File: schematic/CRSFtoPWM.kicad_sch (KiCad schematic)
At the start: 29 parts, among them J1 Bat+, J2 UART1/Rx, J3 ICSP, J4 TSW-104-08-G-T-RA, J5 TSW-104-08-G-T-RA, J6 TSW-104-08-G-T-RA, J7 TSW-102-08-L-T-RA, U1 AP7375-50W5-7, U2 AP2210N-3.3TRG1, U3 ATSAMD21E18A-MU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

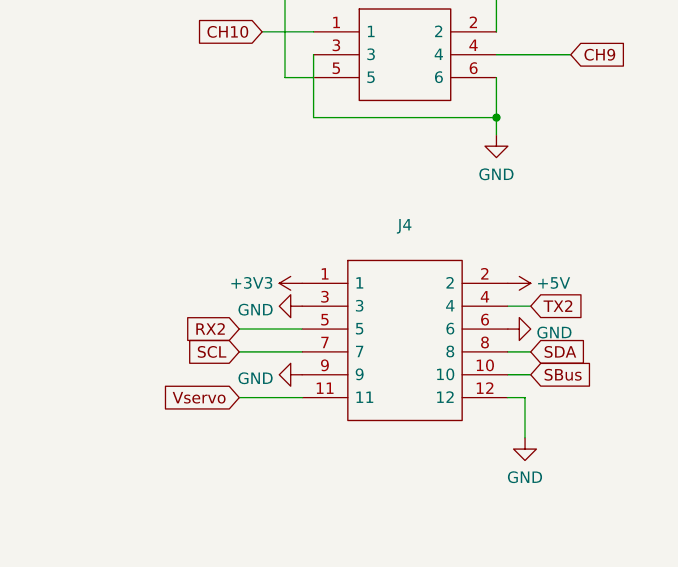
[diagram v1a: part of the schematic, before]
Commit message: Improved Vservo current capacity
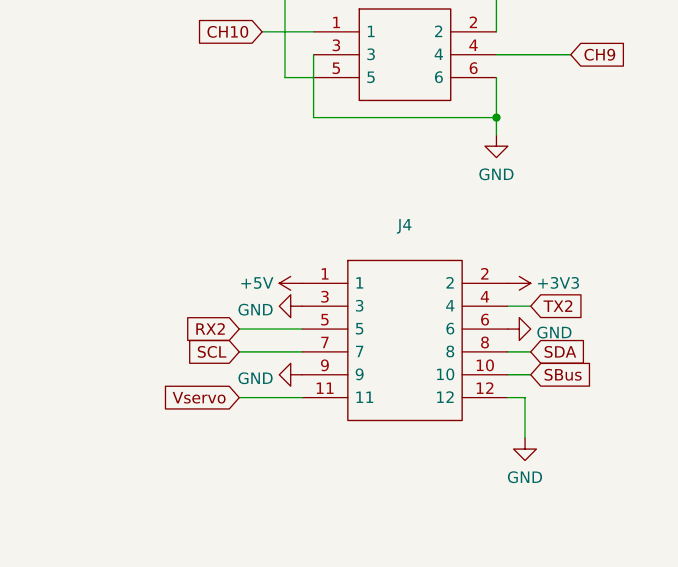
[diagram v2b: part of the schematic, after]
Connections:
- net +3V3: now also J4.2; no longer J4.1
- net +5V: now also J4.1; no longer J4.2
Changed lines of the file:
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@@
     (pin "1")
   )
-  (symbol (lib_id "power:+3V3") (at 222.885 142.875 90) (unit 1)
-    (in_bom yes) (on_board yes)
-    (property "Reference" "#PWR036" (id 0) (at 226.695 142.875 0)
-      (effects (font (size 1.27 1.27)) hide)
-    )
-    (property "Value" "+3V3" (id 1) (at 219.71 142.875 90)
-      (effects (font (size 1.27 1.27)) (justify left))
-    )
-    (property "Footprint" "" (id 2) (at 222.885 142.875 0)
-      (effects (font (size 1.27 1.27)) hide)
-    )
-    (property "Datasheet" "" (id 3) (at 222.885 142.875 0)
+  (symbol (lib_id "power:+3V3") (at 245.745 142.875 270) (unit 1)
+    (in_bom yes) (on_board yes)
+    (property "Reference" "#PWR036" (id 0) (at 241.935 142.875 0)
+      (effects (font (size 1.27 1.27)) hide)
+    )
+    (property "Value" "+3V3" (id 1) (at 248.92 142.875 90)
+      (effects (font (size 1.27 1.27)) (justify left))
+    )
+    (property "Footprint" "" (id 2) (at 245.745 142.875 0)
+      (effects (font (size 1.27 1.27)) hide)
+    )
+    (property "Datasheet" "" (id 3) (at 245.745 142.875 0)
       (effects (font (size 1.27 1.27)) hide)
     )
@@
     (pin "1")
   )
-  (symbol (lib_id "power:+5V") (at 245.745 142.875 270) (unit 1)
-    (in_bom yes) (on_board yes)
-    (property "Reference" "#PWR037" (id 0) (at 241.935 142.875 0)
-      (effects (font (size 1.27 1.27)) hide)
-    )
-    (property "Value" "+5V" (id 1) (at 248.92 142.875 90)
-      (effects (font (size 1.27 1.27)) (justify left))
-    )
-    (property "Footprint" "" (id 2) (at 245.745 142.875 0)
-      (effects (font (size 1.27 1.27)) hide)
-    )
-    (property "Datasheet" "" (id 3) (at 245.745 142.875 0)
-      (effects (font (size 1.27 1.27)) hide)
-    )
+  (symbol (lib_id "power:+5V") (at 222.885 142.875 90) (unit 1)
+    (in_bom yes) (on_board yes)
+    (property "Reference" "#PWR037" (id 0) (at 226.695 142.875 0)
+      (effects (font (size 1.27 1.27)) hide)
+    )
+    (property "Value" "+5V" (id 1) (at 219.71 142.875 90)
+      (effects (font (size 1.27 1.27)) (justify left))
+    )
+    (property "Footprint" "" (id 2) (at 222.885 142.875 0)
+      (effects (font (size 1.27 1.27)) hide)
+    )
+    (property "Datasheet" "" (id 3) (at 222.885 142.875 0)
+      (effects (font (size 1.27 1.27)) hide)
+    )

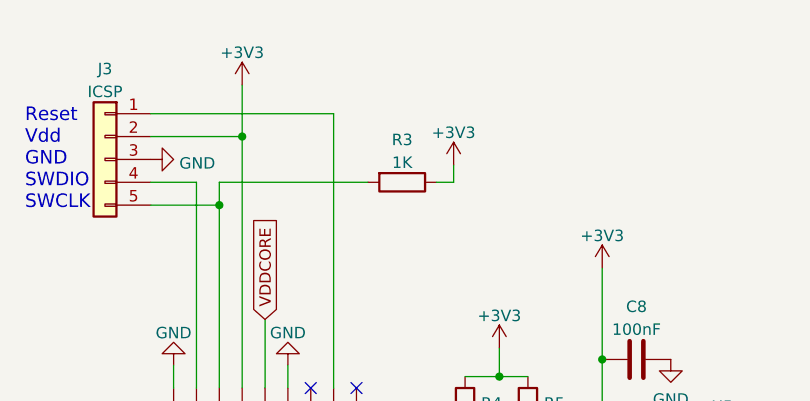
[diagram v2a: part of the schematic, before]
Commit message: Added pullup to RESET
Updated pins in Harmony
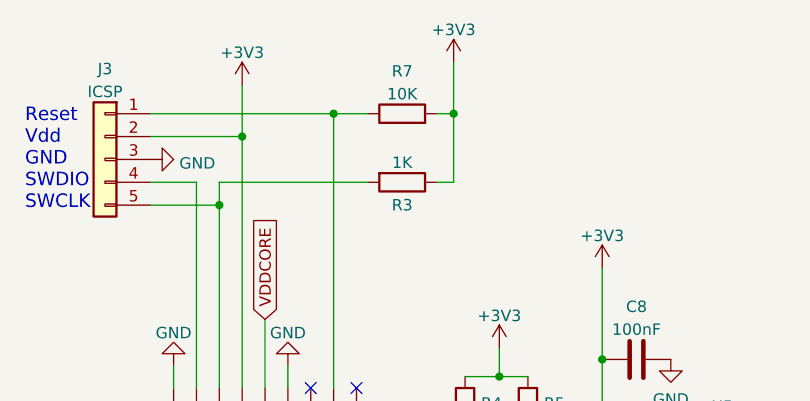
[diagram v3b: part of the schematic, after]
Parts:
- added R7: 10K, Resistor_SMD:R_0603_1608Metric, symbol Device:R
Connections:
- net +3V3: now also R7.2
- net at J3.1 (Pin_1), U3.26 (RESETN): now also R7.1
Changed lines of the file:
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@@
   (title_block
     (title "CRSFtoPWM")
-    (date "2023-01-26")
+    (date "2023-02-04")
     (rev "1.0")
     (company "Quantum Embedded Systems")
@@
   (junction (at 158.115 66.04) (diameter 0) (color 0 0 0 0)
   )
+  (junction (at 138.43 24.765) (diameter 0) (color 0 0 0 0)
+  )
   (junction (at 219.71 53.975) (diameter 0) (color 0 0 0 0)
   )
@@
   )
   (junction (at 219.71 61.595) (diameter 0) (color 0 0 0 0)
+  )
+  (junction (at 151.765 24.765) (diameter 0) (color 0 0 0 0)
   )
   (junction (at 128.27 27.305) (diameter 0) (color 0 0 0 0)
@@
     (stroke (width 0) (type default) (color 0 0 0 0))
   )
+  (wire (pts (xy 138.43 24.765) (xy 142.24 24.765))
+    (stroke (width 0) (type default) (color 0 0 0 0))
+  )
   (wire (pts (xy 223.52 86.995) (xy 222.25 86.995))
     (stroke (width 0) (type default) (color 0 0 0 0))
@@
     (stroke (width 0) (type default) (color 0 0 0 0))
   )
+  (wire (pts (xy 149.86 24.765) (xy 151.765 24.765))
+    (stroke (width 0) (type default) (color 0 0 0 0))
+  )
   (wire (pts (xy 45.72 168.91) (xy 38.1 168.91))
     (stroke (width 0) (type default) (color 0 0 0 0))
@@
     (stroke (width 0) (type default) (color 0 0 0 0))
   )
-  (wire (pts (xy 151.765 30.48) (xy 151.765 32.385))
+  (wire (pts (xy 151.765 19.05) (xy 151.765 24.765))
     (stroke (width 0) (type default) (color 0 0 0 0))
   )
@@
   )
   (wire (pts (xy 234.95 33.655) (xy 234.95 37.465))
+    (stroke (width 0) (type default) (color 0 0 0 0))
+  )
+  (wire (pts (xy 151.765 24.765) (xy 151.765 32.385))
     (stroke (width 0) (type default) (color 0 0 0 0))
   )
@@
   )
   (symbol (lib_id "Device:R") (at 146.05 32.385 270) (unit 1)
-    (in_bom yes) (on_board yes) (fields_autoplaced)
-    (property "Reference" "R3" (id 0) (at 146.05 27.6692 90))
+    (in_bom yes) (on_board yes)
+    (property "Reference" "R3" (id 0) (at 146.05 34.925 90))
     (property "Value" "1K" (id 1) (at 146.05 30.2061 90))
     (property "Footprint" "Resistor_SMD:R_0603_1608Metric" (id 2) (at 146.05 30.607 90)
@@
     )
     (pin "1")
+  )
+  (symbol (lib_id "Device:R") (at 146.05 24.765 90) (unit 1)
+    (in_bom yes) (on_board yes) (fields_autoplaced)
+    (property "Reference" "R7" (id 0) (at 146.05 20.0492 90))
+    (property "Value" "10K" (id 1) (at 146.05 22.5861 90))
+    (property "Footprint" "Resistor_SMD:R_0603_1608Metric" (id 2) (at 146.05 26.543 90)
+      (effects (font (size 1.27 1.27)) hide)
+    )
+    (property "Datasheet" "~" (id 3) (at 146.05 24.765 0)
+      (effects (font (size 1.27 1.27)) hide)
+    )
+    (pin "1")
+    (pin "2")
   )
   (symbol (lib_id "Connector_Generic:Conn_01x05") (at 113.03 29.845 0) (mirror y) (unit 1)
@@
     (pin "1")
   )
-  (symbol (lib_id "power:+3V3") (at 151.765 30.48 0) (unit 1)
+  (symbol (lib_id "power:+3V3") (at 151.765 19.05 0) (unit 1)
     (in_bom yes) (on_board yes)
-    (property "Reference" "#PWR023" (id 0) (at 151.765 34.29 0)
-      (effects (font (size 1.27 1.27)) hide)
-    )
-    (property "Value" "+3V3" (id 1) (at 151.765 26.8755 0))
-    (property "Footprint" "" (id 2) (at 151.765 30.48 0)
-      (effects (font (size 1.27 1.27)) hide)
-    )
-    (property "Datasheet" "" (id 3) (at 151.765 30.48 0)
+    (property "Reference" "#PWR023" (id 0) (at 151.765 22.86 0)
+      (effects (font (size 1.27 1.27)) hide)
+    )
+    (property "Value" "+3V3" (id 1) (at 151.765 15.4455 0))
+    (property "Footprint" "" (id 2) (at 151.765 19.05 0)
+      (effects (font (size 1.27 1.27)) hide)
+    )
+    (property "Datasheet" "" (id 3) (at 151.765 19.05 0)
       (effects (font (size 1.27 1.27)) hide)
     )
@@
       (reference "R6") (unit 1) (value "1K") (footprint "Resistor_SMD:R_0603_1608Metric")
     )
+    (path "/5b2872c0-f13d-4bc9-8d17-c9265e155041"
+      (reference "R7") (unit 1) (value "10K") (footprint "Resistor_SMD:R_0603_1608Metric")
+    )
     (path "/41207f5d-a88b-4d8b-a31d-fbc7ed62322f"

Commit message: Made labels consistent
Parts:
- C1, C2: value 100n -> 100nF
- C3, C6: value 10 uF -> 10uF
- C4, C5: value 1 uF -> 1uF
- C7: value 2.2 uF -> 2.2uF
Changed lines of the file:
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@@
   (symbol (lib_id "Device:C") (at 80.01 140.97 0) (unit 1)
     (in_bom yes) (on_board yes) (fields_autoplaced)
-    (property "Reference" "C7" (id 0) (at 82.931 140.0615 0)
-      (effects (font (size 1.27 1.27)) (justify left))
-    )
-    (property "Value" "2.2 uF" (id 1) (at 82.931 142.8366 0)
+    (property "Reference" "C7" (id 0) (at 82.931 140.1353 0)
+      (effects (font (size 1.27 1.27)) (justify left))
+    )
+    (property "Value" "2.2uF" (id 1) (at 82.931 142.6722 0)
       (effects (font (size 1.27 1.27)) (justify left))
     )
@@
   (symbol (lib_id "Device:C") (at 43.18 177.8 0) (unit 1)
     (in_bom yes) (on_board yes) (fields_autoplaced)
-    (property "Reference" "C4" (id 0) (at 46.101 176.8915 0)
-      (effects (font (size 1.27 1.27)) (justify left))
-    )
-    (property "Value" "1 uF" (id 1) (at 46.101 179.6666 0)
+    (property "Reference" "C4" (id 0) (at 46.101 176.9653 0)
+      (effects (font (size 1.27 1.27)) (justify left))
+    )
+    (property "Value" "1uF" (id 1) (at 46.101 179.5022 0)
       (effects (font (size 1.27 1.27)) (justify left))
     )
@@
       (effects (font (size 1.27 1.27)) (justify left))
     )
-    (property "Value" "1 uF" (id 1) (at 68.961 44.958 0)
+    (property "Value" "1uF" (id 1) (at 68.961 44.958 0)
       (effects (font (size 1.27 1.27)) (justify left))
     )
@@
       (effects (font (size 1.27 1.27)) (justify left))
     )
-    (property "Value" "100n" (id 1) (at 45.466 48.133 0)
+    (property "Value" "100nF" (id 1) (at 45.466 48.133 0)
       (effects (font (size 1.27 1.27)) (justify left))
     )
@@
   (symbol (lib_id "Device:C") (at 43.18 140.97 0) (unit 1)
     (in_bom yes) (on_board yes) (fields_autoplaced)
-    (property "Reference" "C3" (id 0) (at 46.101 140.0615 0)
-      (effects (font (size 1.27 1.27)) (justify left))
-    )
-    (property "Value" "10 uF" (id 1) (at 46.101 142.8366 0)
+    (property "Reference" "C3" (id 0) (at 46.101 140.1353 0)
+      (effects (font (size 1.27 1.27)) (justify left))
+    )
+    (property "Value" "10uF" (id 1) (at 46.101 142.6722 0)
       (effects (font (size 1.27 1.27)) (justify left))
     )
@@
   (symbol (lib_id "Device:C") (at 76.2 177.8 0) (unit 1)
     (in_bom yes) (on_board yes) (fields_autoplaced)
-    (property "Reference" "C6" (id 0) (at 79.121 176.8915 0)
-      (effects (font (size 1.27 1.27)) (justify left))
-    )
-    (property "Value" "10 uF" (id 1) (at 79.121 179.6666 0)
+    (property "Reference" "C6" (id 0) (at 79.121 176.9653 0)
+      (effects (font (size 1.27 1.27)) (justify left))
+    )
+    (property "Value" "10uF" (id 1) (at 79.121 179.5022 0)
       (effects (font (size 1.27 1.27)) (justify left))
     )
@@
       (effects (font (size 1.27 1.27)) (justify left))
     )
-    (property "Value" "100n" (id 1) (at 32.766 40.513 0)
+    (property "Value" "100nF" (id 1) (at 32.766 40.513 0)
       (effects (font (size 1.27 1.27)) (justify left))
     )
@@
     )
     (path "/8e9103e6-5cca-4319-9d48-d0ef350c6eca"
-      (reference "C1") (unit 1) (value "100n") (footprint "Capacitor_SMD:C_0402_1005Metric")
+      (reference "C1") (unit 1) (value "100nF") (footprint "Capacitor_SMD:C_0402_1005Metric")
     )
     (path "/3d7a82a5-d454-4843-a436-aa14b35819cc"
-      (reference "C2") (unit 1) (value "100n") (footprint "Capacitor_SMD:C_0402_1005Metric")
+      (reference "C2") (unit 1) (value "100nF") (footprint "Capacitor_SMD:C_0402_1005Metric")
     )
     (path "/5cffb795-e778-4eab-a812-6dcf084529ee"
-      (reference "C3") (unit 1) (value "10 uF") (footprint "Capacitor_SMD:C_0603_1608Metric")
+      (reference "C3") (unit 1) (value "10uF") (footprint "Capacitor_SMD:C_0603_1608Metric")
     )
     (path "/2705eb2f-fbe1-4caa-886d-407f7836ed33"
-      (reference "C4") (unit 1) (value "1 uF") (footprint "Capacitor_SMD:C_0603_1608Metric")
+      (reference "C4") (unit 1) (value "1uF") (footprint "Capacitor_SMD:C_0603_1608Metric")
     )
     (path "/2f8f1993-d601-4571-92e3-038995044650"
-      (reference "C5") (unit 1) (value "1 uF") (footprint "Capacitor_SMD:C_0402_1005Metric")
+      (reference "C5") (unit 1) (value "1uF") (footprint "Capacitor_SMD:C_0402_1005Metric")
     )
     (path "/66e4372c-7537-4142-839f-eb8ca3b54f14"
-      (reference "C6") (unit 1) (value "10 uF") (footprint "Capacitor_SMD:C_0603_1608Metric")
+      (reference "C6") (unit 1) (value "10uF") (footprint "Capacitor_SMD:C_0603_1608Metric")
     )
     (path "/0167b6e5-6854-4193-b6f3-8c2579085159"
-      (reference "C7") (unit 1) (value "2.2 uF") (footprint "Capacitor_SMD:C_0603_1608Metric")
+      (reference "C7") (unit 1) (value "2.2uF") (footprint "Capacitor_SMD:C_0603_1608Metric")
     )
     (path "/45a09faa-6dbe-41f1-b47a-cd399891ea4f"

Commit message: Updated schematic to correct channel numbering
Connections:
- net CH1: now also J5.10, U3.7 (PA06); no longer J5.4, U3.11 (PA08)
- net CH2: now also J5.7, U3.8 (PA07); no longer J5.1, U3.12 (PA09)
- net CH3: now also J5.4, U3.11 (PA08); no longer J6.10, U3.13 (PA10)
- net CH4: now also J5.1, U3.12 (PA09); no longer J6.7, U3.14 (PA11)
- net CH5: now also J6.10, U3.13 (PA10); no longer J5.10, U3.7 (PA06)
- net CH6: now also J6.7, U3.14 (PA11); no longer J5.7, U3.8 (PA07)
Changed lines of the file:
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@@
     )
   )
-  (global_label "CH2" (shape input) (at 215.265 48.895 180) (fields_autoplaced)
+  (global_label "CH4" (shape input) (at 215.265 48.895 180) (fields_autoplaced)
     (effects (font (size 1.27 1.27)) (justify right))
     (property "Intersheet References" "${INTERSHEET_REFS}" (id 0) (at 209.0419 48.8156 0)
@@
     )
   )
-  (global_label "CH1" (shape input) (at 255.27 51.435 0) (fields_autoplaced)
+  (global_label "CH3" (shape input) (at 255.27 51.435 0) (fields_autoplaced)
     (effects (font (size 1.27 1.27)) (justify left))
     (property "Intersheet References" "${INTERSHEET_REFS}" (id 0) (at 261.4931 51.3556 0)
@@
     )
   )
-  (global_label "CH6" (shape input) (at 215.265 56.515 180) (fields_autoplaced)
+  (global_label "CH2" (shape input) (at 215.265 56.515 180) (fields_autoplaced)
     (effects (font (size 1.27 1.27)) (justify right))
     (property "Intersheet References" "${INTERSHEET_REFS}" (id 0) (at 209.0419 56.4356 0)
@@
     )
   )
-  (global_label "CH4" (shape input) (at 133.35 120.65 270) (fields_autoplaced)
+  (global_label "CH6" (shape input) (at 133.35 120.65 270) (fields_autoplaced)
     (effects (font (size 1.27 1.27)) (justify right))
     (property "Intersheet References" "${INTERSHEET_REFS}" (id 0) (at 133.2706 126.8731 90)
@@
     )
   )
-  (global_label "CH4" (shape input) (at 215.265 84.455 180) (fields_autoplaced)
+  (global_label "CH6" (shape input) (at 215.265 84.455 180) (fields_autoplaced)
     (effects (font (size 1.27 1.27)) (justify right))
     (property "Intersheet References" "${INTERSHEET_REFS}" (id 0) (at 209.0419 84.3756 0)
@@
     )
   )
-  (global_label "CH5" (shape input) (at 106.045 101.6 270) (fields_autoplaced)
+  (global_label "CH1" (shape input) (at 106.045 101.6 270) (fields_autoplaced)
     (effects (font (size 1.27 1.27)) (justify right))
     (property "Intersheet References" "${INTERSHEET_REFS}" (id 0) (at 105.9656 107.8231 90)
@@
     )
   )
-  (global_label "CH1" (shape input) (at 125.73 120.65 270) (fields_autoplaced)
+  (global_label "CH3" (shape input) (at 125.73 120.65 270) (fields_autoplaced)
     (effects (font (size 1.27 1.27)) (justify right))
     (property "Intersheet References" "${INTERSHEET_REFS}" (id 0) (at 125.6506 126.8731 90)
@@
     )
   )
-  (global_label "CH6" (shape input) (at 109.22 101.6 270) (fields_autoplaced)
+  (global_label "CH2" (shape input) (at 109.22 101.6 270) (fields_autoplaced)
     (effects (font (size 1.27 1.27)) (justify right))
     (property "Intersheet References" "${INTERSHEET_REFS}" (id 0) (at 109.1406 107.8231 90)
@@
     )
   )
-  (global_label "CH3" (shape input) (at 255.27 86.995 0) (fields_autoplaced)
+  (global_label "CH5" (shape input) (at 255.27 86.995 0) (fields_autoplaced)
     (effects (font (size 1.27 1.27)) (justify left))
     (property "Intersheet References" "${INTERSHEET_REFS}" (id 0) (at 261.4931 86.9156 0)
@@
     )
   )
-  (global_label "CH2" (shape input) (at 128.27 120.65 270) (fields_autoplaced)
+  (global_label "CH4" (shape input) (at 128.27 120.65 270) (fields_autoplaced)
     (effects (font (size 1.27 1.27)) (justify right))
     (property "Intersheet References" "${INTERSHEET_REFS}" (id 0) (at 128.1906 126.8731 90)
@@
     )
   )
-  (global_label "CH3" (shape input) (at 130.81 120.65 270) (fields_autoplaced)
+  (global_label "CH5" (shape input) (at 130.81 120.65 270) (fields_autoplaced)
     (effects (font (size 1.27 1.27)) (justify right))
     (property "Intersheet References" "${INTERSHEET_REFS}" (id 0) (at 130.7306 126.8731 90)
@@
     )
   )
-  (global_label "CH5" (shape input) (at 255.27 59.055 0) (fields_autoplaced)
+  (global_label "CH1" (shape input) (at 255.27 59.055 0) (fields_autoplaced)
     (effects (font (size 1.27 1.27)) (justify left))
     (property "Intersheet References" "${INTERSHEET_REFS}" (id 0) (at 261.4931 58.9756 0)

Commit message: Changed power circuit
3.3V regulator now uses regulated 5V for input.  Less load on 3.3V regulator and only the 5V regulator has high voltage input.
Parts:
- C4: footprint Capacitor_SMD:C_0603_1608Metric -> Capacitor_SMD:C_0805_2012Metric
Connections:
- net +5V: now also C3.1, U2.3 (VIN)
- net Vbat: no longer C3.1, U2.3 (VIN)
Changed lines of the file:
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@@
     (stroke (width 0) (type default) (color 0 0 0 0))
   )
-  (wire (pts (xy 39.37 134.62) (xy 43.18 134.62))
+  (wire (pts (xy 37.465 134.62) (xy 43.18 134.62))
     (stroke (width 0) (type default) (color 0 0 0 0))
   )
@@
   )
   (wire (pts (xy 172.085 134.62) (xy 172.085 140.97))
+    (stroke (width 0) (type default) (color 0 0 0 0))
+  )
+  (wire (pts (xy 37.465 134.62) (xy 37.465 132.08))
     (stroke (width 0) (type default) (color 0 0 0 0))
   )
@@
     )
   )
-  (global_label "Vbat" (shape input) (at 39.37 134.62 180) (fields_autoplaced)
-    (effects (font (size 1.27 1.27)) (justify right))
-    (property "Intersheet References" "${INTERSHEET_REFS}" (id 0) (at 32.8445 134.5406 0)
-      (effects (font (size 1.27 1.27)) (justify right) hide)
-    )
-  )
   (global_label "CH10" (shape input) (at 218.44 114.935 180) (fields_autoplaced)
     (effects (font (size 1.27 1.27)) (justify right))
@@
       (effects (font (size 1.27 1.27)) (justify left))
     )
-    (property "Footprint" "Capacitor_SMD:C_0603_1608Metric" (id 2) (at 44.1452 181.61 0)
+    (property "Footprint" "Capacitor_SMD:C_0805_2012Metric" (id 2) (at 44.1452 181.61 0)
       (effects (font (size 1.27 1.27)) hide)
     )
@@
     (pin "4")
     (pin "5")
+  )
+  (symbol (lib_id "power:+5V") (at 37.465 132.08 0) (unit 1)
+    (in_bom yes) (on_board yes) (fields_autoplaced)
+    (property "Reference" "#PWR0102" (id 0) (at 37.465 135.89 0)
+      (effects (font (size 1.27 1.27)) hide)
+    )
+    (property "Value" "+5V" (id 1) (at 37.465 128.5042 0))
+    (property "Footprint" "" (id 2) (at 37.465 132.08 0)
+      (effects (font (size 1.27 1.27)) hide)
+    )
+    (property "Datasheet" "" (id 3) (at 37.465 132.08 0)
+      (effects (font (size 1.27 1.27)) hide)
+    )
+    (pin "1")
   )
   (symbol (lib_id "Device:R") (at 146.05 32.385 270) (unit 1)
@@
       (reference "#PWR0101") (unit 1) (value "GND") (footprint "")
     )
+    (path "/4254a4c6-e2e3-48ad-8de6-e8541a3fdbbb"
+      (reference "#PWR0102") (unit 1) (value "+5V") (footprint "")
+    )
     (path "/8e9103e6-5cca-4319-9d48-d0ef350c6eca"
       (reference "C1") (unit 1) (value "100nF") (footprint "Capacitor_SMD:C_0402_1005Metric")
@@
     )
     (path "/2705eb2f-fbe1-4caa-886d-407f7836ed33"
-      (reference "C4") (unit 1) (value "1uF") (footprint "Capacitor_SMD:C_0603_1608Metric")
+      (reference "C4") (unit 1) (value "1uF") (footprint "Capacitor_SMD:C_0805_2012Metric")
     )
     (path "/2f8f1993-d601-4571-92e3-038995044650"

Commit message: Changed input cap back to 0603 and new gerbers
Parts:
- C4: footprint Capacitor_SMD:C_0805_2012Metric -> Capacitor_SMD:C_0603_1608Metric
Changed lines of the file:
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@@
       (effects (font (size 1.27 1.27)) (justify left))
     )
-    (property "Footprint" "Capacitor_SMD:C_0805_2012Metric" (id 2) (at 44.1452 181.61 0)
+    (property "Footprint" "Capacitor_SMD:C_0603_1608Metric" (id 2) (at 44.1452 181.61 0)
       (effects (font (size 1.27 1.27)) hide)
     )
@@
     )
     (path "/2705eb2f-fbe1-4caa-886d-407f7836ed33"
-      (reference "C4") (unit 1) (value "1uF") (footprint "Capacitor_SMD:C_0805_2012Metric")
+      (reference "C4") (unit 1) (value "1uF") (footprint "Capacitor_SMD:C_0603_1608Metric")
     )
     (path "/2f8f1993-d601-4571-92e3-038995044650"
